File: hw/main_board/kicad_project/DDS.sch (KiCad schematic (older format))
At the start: 0 parts

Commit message: refactored schematic, finalized gain/range
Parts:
- added C? (x5): 0.1uF, symbol C
- added C? (x2): 1uF, symbol C
- added C?: 0.01uF, symbol C
- added C? (x2): 20pF, symbol C
- added DDS?: AD9838, symbol AD9838
- added R?: 20K, symbol R
- added R? (x2): 137R, symbol R
- added RV?: 1K, symbol POT
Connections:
- new net: C?.2, DDS?.3 (DCAP/2.5V)
- new net: C?.1, DDS?.20 (COMP)
- new net: C?.2, DDS?.18 (FSADJUST), R?.1
- new net: C?.1, DDS?.19 (REFOUT)
- new net: R?.2, RV?.1, RV?.2
- new net AGND: C?.1, C?.1, C?.1, C?.1, C?.1, C?.2, C?.2, C?.2, C?.2, DDS?.15 (AGND), DDS?.4 (DGND), R?.1, R?.1, RV?.3
- new net AVDD_3V3: C?.2, C?.2, C?.2, DDS?.1 (AVDD)
- new net CLK_IN: DDS?.5 (MCLK)
- new net DDS_BUS0: DDS?.10 (SDATA)
- new net DDS_BUS1: DDS?.11 (SCLK)
- new net DDS_BUS2: DDS?.12 (FSYNC)
- new net DDS_BUS3: DDS?.6 (FSELECT)
- new net DDS_BUS4: DDS?.7 (PSELECT)
- new net DDS_BUS5: DDS?.8 (RESET)
- new net DDS_BUS6: DDS?.9 (SLEEP)
- new net DVDD_3V3: C?.1, C?.2, DDS?.2 (DVDD)
- new net VOut: C?.1, DDS?.16 (IOUT), R?.2
- new net VOut-: C?.1, DDS?.17 (IOUTB), R?.2

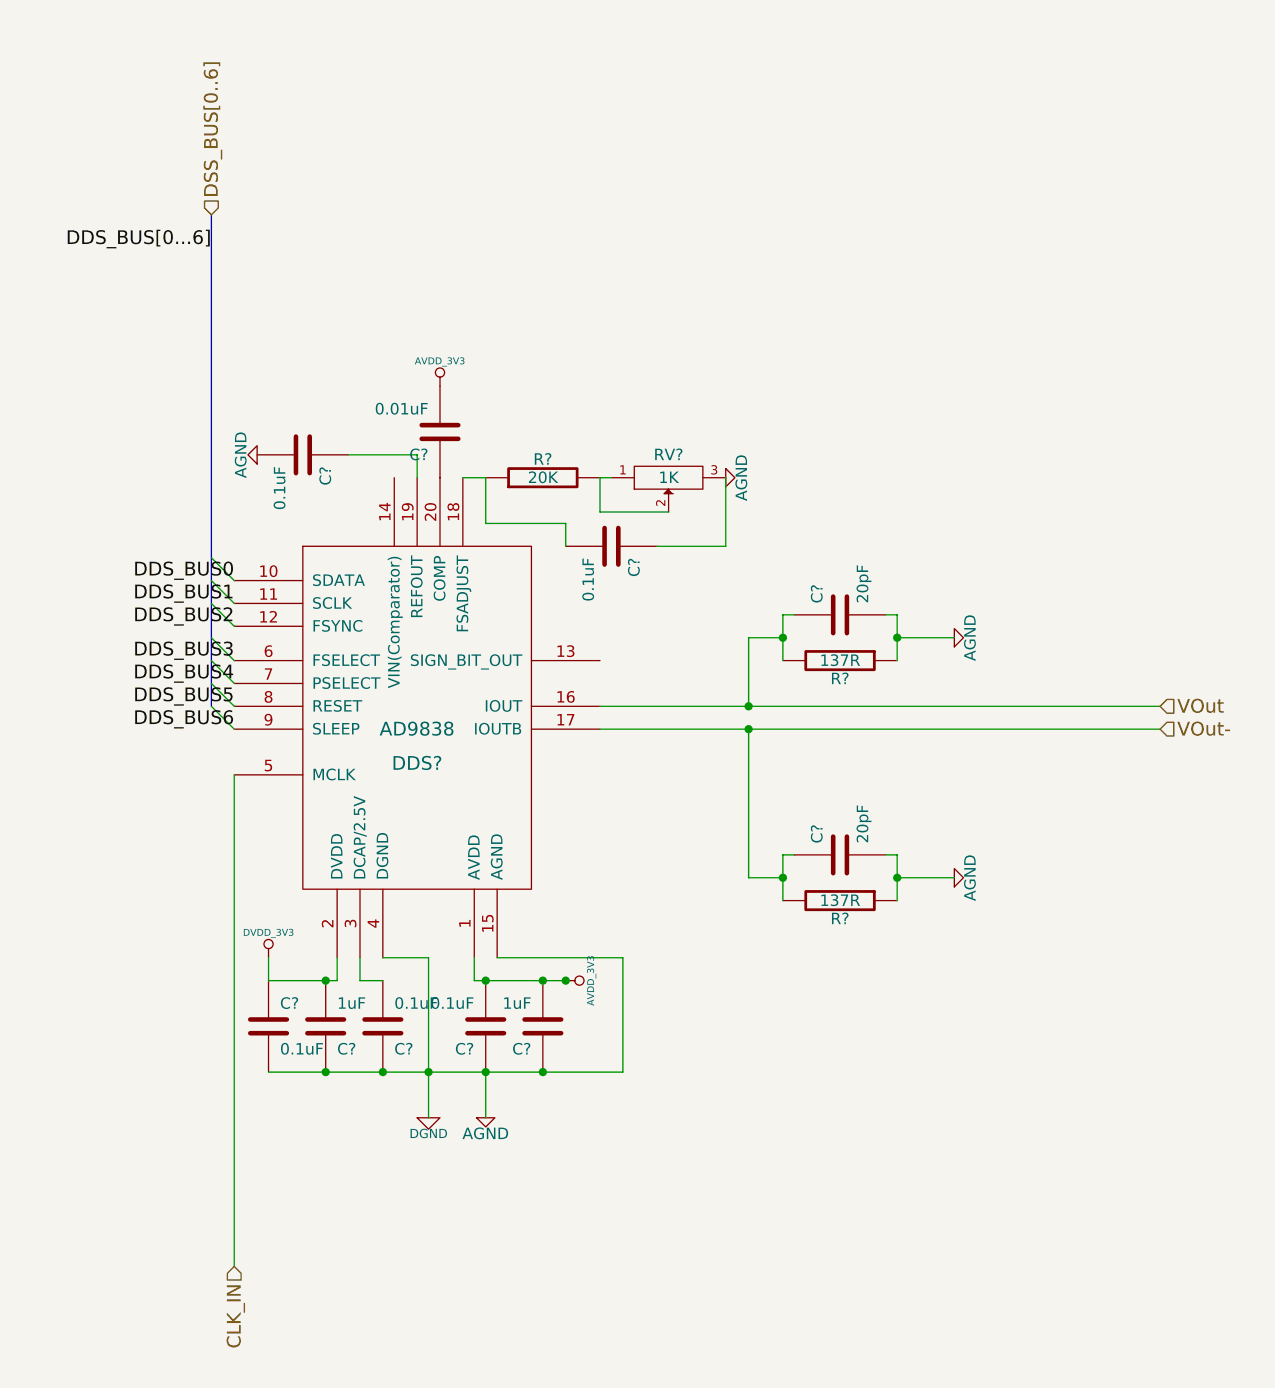
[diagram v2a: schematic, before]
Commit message: started mainboard pcb layout, fixing small things in schematic, TODO: schematic connector symbols and pads
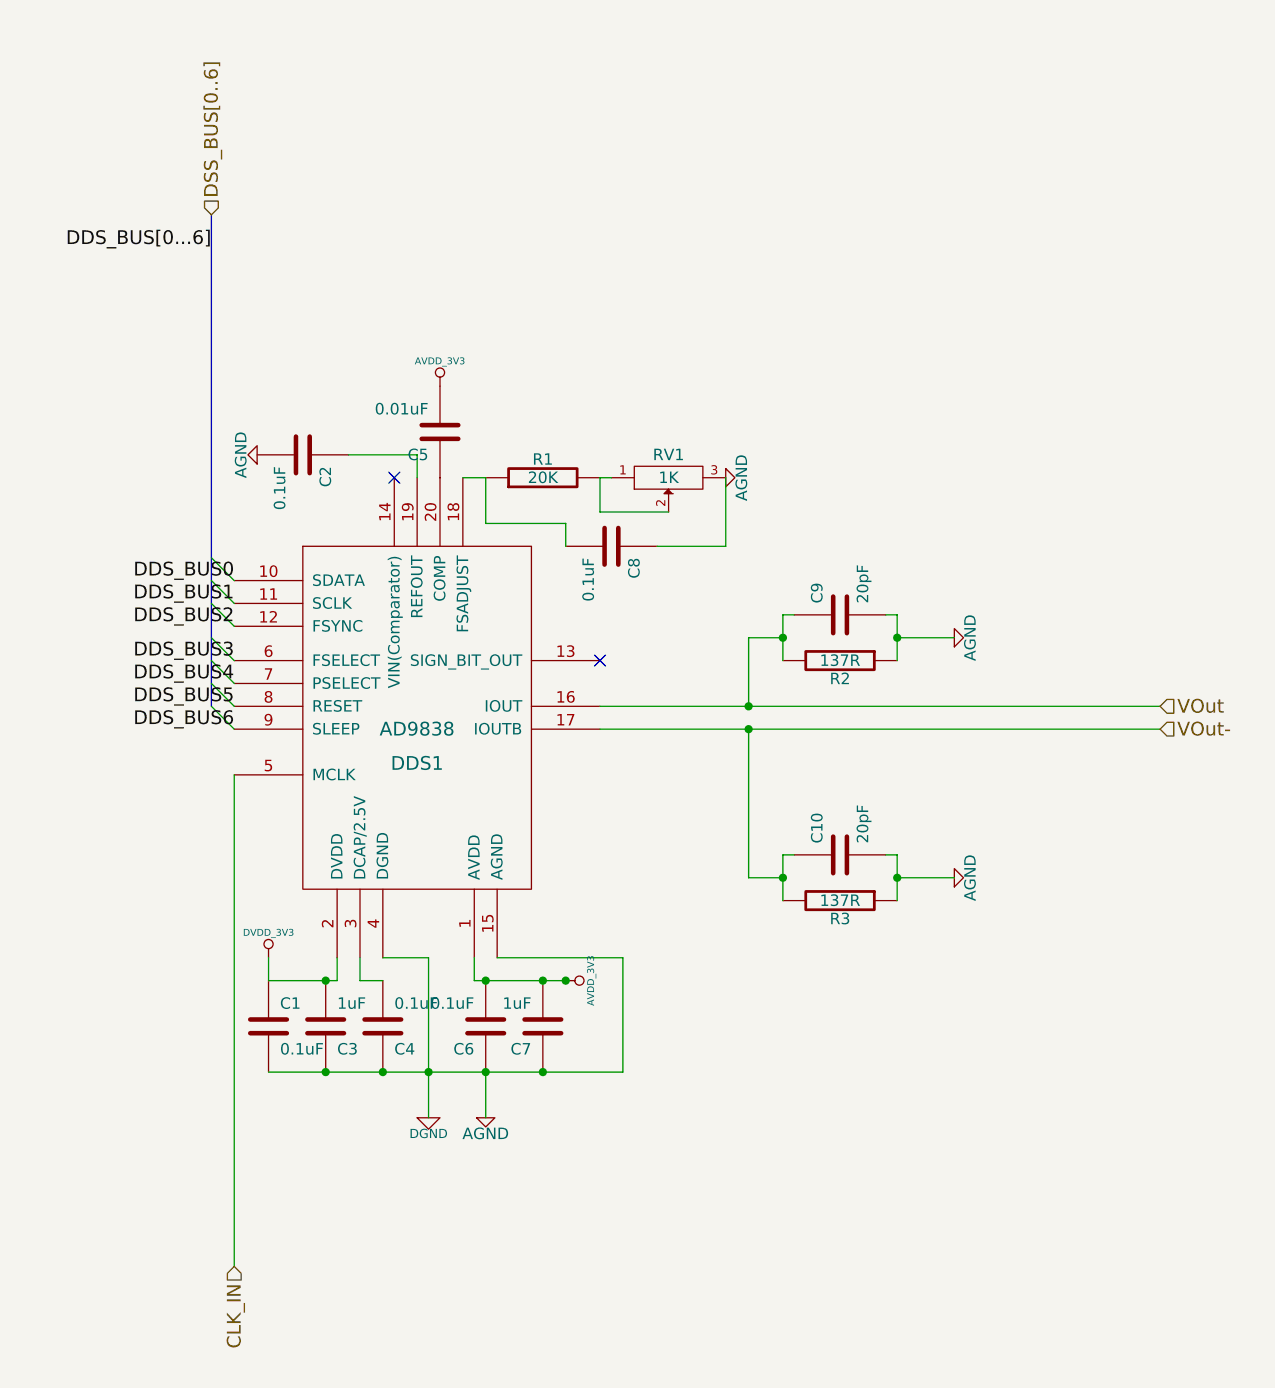
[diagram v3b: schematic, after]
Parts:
- C1, C10, C2, C3, C4, C5, C6, C7, C8, C9: renamed from C?; footprint (none) -> 0603
- DDS1: renamed from DDS?; footprint (none) -> LFCSP20_WQ
- R1, R2, R3: renamed from R?; footprint (none) -> 0603
- RV1: renamed from RV?; footprint (none) -> 3224X
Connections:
- no-connect marks 0 -> 2
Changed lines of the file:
@@
 encoding utf-8
 Sheet 4 7
-Title ""
-Date ""
-Rev ""
+Title "DDS Stage"
+Date "01 Feb 2014"
+Rev "A"
 Comp ""
-Comment1 ""
+Comment1 "Copyright 2014 Andrey Shmakov"
 Comment2 ""
 Comment3 ""
@@
 	5700 4650 5700 5350
 $Comp
-L AGND #PWR?
+L AGND #PWR018
 U 1 1 53166330
 P 5950 5350
-F 0 "#PWR?" H 5950 5350 40  0001 C CNN
+F 0 "#PWR018" H 5950 5350 40  0001 C CNN
 F 1 "AGND" H 5950 5280 50  0000 C CNN
 F 2 "" H 5950 5350 60  0001 C CNN
@@
 $EndComp
 $Comp
-L DGND #PWR?
+L DGND #PWR019
 U 1 1 53166336
 P 5700 5350
-F 0 "#PWR?" H 5700 5350 40  0001 C CNN
+F 0 "#PWR019" H 5700 5350 40  0001 C CNN
 F 1 "DGND" H 5700 5280 40  0000 C CNN
 F 2 "" H 5700 5350 60  0001 C CNN
@@
 $EndComp
 $Comp
-L AVDD_3V3 #PWR?
+L AVDD_3V3 #PWR020
 U 1 1 5316633C
 P 6300 4750
-F 0 "#PWR?" H 6300 4850 30  0001 C CNN
+F 0 "#PWR020" H 6300 4850 30  0001 C CNN
 F 1 "AVDD_3V3" H 6300 4860 30  0000 C CNN
 F 2 "" H 6300 4750 60  0001 C CNN
@@
 $EndComp
 $Comp
-L DVDD_3V3 #PWR?
+L DVDD_3V3 #PWR021
 U 1 1 53166342
 P 5000 4650
-F 0 "#PWR?" H 5000 4750 30  0001 C CNN
+F 0 "#PWR021" H 5000 4750 30  0001 C CNN
 F 1 "DVDD_3V3" H 5000 4760 30  0000 C CNN
 F 2 "" H 5000 4650 60  0001 C CNN
@@
 $EndComp
 $Comp
-L C C?
+L C C4
 U 1 1 53166348
 P 5500 4950
-F 0 "C?" H 5550 5050 50  0000 L CNN
+F 0 "C4" H 5550 5050 50  0000 L CNN
 F 1 "0.1uF" H 5550 4850 50  0000 L CNN
-F 2 "" H 5500 4950 60  0001 C CNN
+F 2 "0603" H 5500 4950 60  0001 C CNN
 F 3 "" H 5500 4950 60  0001 C CNN
 	1    5500 4950
@@
 $EndComp
 $Comp
-L C C?
+L C C3
 U 1 1 5316634E
 P 5250 4950
-F 0 "C?" H 5300 5050 50  0000 L CNN
+F 0 "C3" H 5300 5050 50  0000 L CNN
 F 1 "1uF" H 5300 4850 50  0000 L CNN
-F 2 "" H 5250 4950 60  0001 C CNN
+F 2 "0603" H 5250 4950 60  0001 C CNN
 F 3 "" H 5250 4950 60  0001 C CNN
 	1    5250 4950
@@
 $EndComp
 $Comp
-L C C?
+L C C1
 U 1 1 53166354
 P 5000 4950
-F 0 "C?" H 5050 5050 50  0000 L CNN
+F 0 "C1" H 5050 5050 50  0000 L CNN
 F 1 "0.1uF" H 5050 4850 50  0000 L CNN
-F 2 "" H 5000 4950 60  0001 C CNN
+F 2 "0603" H 5000 4950 60  0001 C CNN
 F 3 "" H 5000 4950 60  0001 C CNN
 	1    5000 4950
@@
 $EndComp
 $Comp
-L AVDD_3V3 #PWR?
+L AVDD_3V3 #PWR022
 U 1 1 5316635A
 P 5750 2150
-F 0 "#PWR?" H 5750 2250 30  0001 C CNN
+F 0 "#PWR022" H 5750 2250 30  0001 C CNN
 F 1 "AVDD_3V3" H 5750 2260 30  0000 C CNN
 F 2 "" H 5750 2150 60  0001 C CNN
@@
 $EndComp
 $Comp
-L C C?
+L C C5
 U 1 1 53166360
 P 5750 2350
-F 0 "C?" H 5800 2450 50  0000 L CNN
+F 0 "C5" H 5800 2450 50  0000 L CNN
 F 1 "0.01uF" H 5800 2250 50  0000 L CNN
-F 2 "" H 5750 2350 60  0001 C CNN
+F 2 "0603" H 5750 2350 60  0001 C CNN
 F 3 "" H 5750 2350 60  0001 C CNN
 	1    5750 2350
@@
 $EndComp
 $Comp
-L C C?
+L C C7
 U 1 1 53166372
 P 6200 4950
-F 0 "C?" H 6250 5050 50  0000 L CNN
+F 0 "C7" H 6250 5050 50  0000 L CNN
 F 1 "1uF" H 6250 4850 50  0000 L CNN
-F 2 "" H 6200 4950 60  0001 C CNN
+F 2 "0603" H 6200 4950 60  0001 C CNN
 F 3 "" H 6200 4950 60  0001 C CNN
 	1    6200 4950
@@
 $EndComp
 $Comp
-L C C?
+L C C6
 U 1 1 53166378
 P 5950 4950
-F 0 "C?" H 6000 5050 50  0000 L CNN
+F 0 "C6" H 6000 5050 50  0000 L CNN
 F 1 "0.1uF" H 6000 4850 50  0000 L CNN
-F 2 "" H 5950 4950 60  0001 C CNN
+F 2 "0603" H 5950 4950 60  0001 C CNN
 F 3 "" H 5950 4950 60  0001 C CNN
 	1    5950 4950
@@
 Connection ~ 6300 4750
 $Comp
-L R R?
+L R R1
 U 1 1 531663A9
 P 6200 2550
-F 0 "R?" V 6280 2550 50  0000 C CNN
+F 0 "R1" V 6280 2550 50  0000 C CNN
 F 1 "20K" V 6200 2550 50  0000 C CNN
-F 2 "" H 6200 2550 60  0001 C CNN
+F 2 "0603" H 6200 2550 60  0001 C CNN
 F 3 "" H 6200 2550 60  0001 C CNN
 	1    6200 2550
@@
 $EndComp
 $Comp
-L POT RV?
+L POT RV1
 U 1 1 531663AF
 P 6750 2550
-F 0 "RV?" H 6750 2450 50  0000 C CNN
+F 0 "RV1" H 6750 2450 50  0000 C CNN
 F 1 "1K" H 6750 2550 50  0000 C CNN
-F 2 "" H 6750 2550 60  0001 C CNN
+F 2 "3224X" H 6750 2550 60  0001 C CNN
 F 3 "" H 6750 2550 60  0001 C CNN
 	1    6750 2550
@@
 	6450 2700 6450 2550
 $Comp
-L AGND #PWR?
+L AGND #PWR023
 U 1 1 531663B9
 P 7000 2550
-F 0 "#PWR?" H 7000 2550 40  0001 C CNN
+F 0 "#PWR023" H 7000 2550 40  0001 C CNN
 F 1 "AGND" H 7000 2480 50  0000 C CNN
 F 2 "" H 7000 2550 60  0001 C CNN
@@
 $EndComp
 $Comp
-L C C?
+L C C8
 U 1 1 531663BF
 P 6500 2850
-F 0 "C?" H 6550 2950 50  0000 L CNN
+F 0 "C8" H 6550 2950 50  0000 L CNN
 F 1 "0.1uF" H 6550 2750 50  0000 L CNN
-F 2 "" H 6500 2850 60  0001 C CNN
+F 2 "0603" H 6500 2850 60  0001 C CNN
 F 3 "" H 6500 2850 60  0001 C CNN
 	1    6500 2850
@@
 	7000 2850 7000 2550
 $Comp
-L C C?
+L C C2
 U 1 1 531663CA
 P 5150 2450
-F 0 "C?" H 5200 2550 50  0000 L CNN
+F 0 "C2" H 5200 2550 50  0000 L CNN
 F 1 "0.1uF" H 5200 2350 50  0000 L CNN
-F 2 "" H 5150 2450 60  0001 C CNN
+F 2 "0603" H 5150 2450 60  0001 C CNN
 F 3 "" H 5150 2450 60  0001 C CNN
 	1    5150 2450
@@
 	5650 2450 5350 2450
 $Comp
-L AGND #PWR?
+L AGND #PWR024
 U 1 1 531663D2
 P 4950 2450
-F 0 "#PWR?" H 4950 2450 40  0001 C CNN
+F 0 "#PWR024" H 4950 2450 40  0001 C CNN
 F 1 "AGND" H 4950 2380 50  0000 C CNN
 F 2 "" H 4950 2450 60  0001 C CNN
@@
 DSS_BUS[0..6]
 $Comp
-L C C?
+L C C9
 U 1 1 53166A22
 P 7500 3150
-F 0 "C?" H 7550 3250 50  0000 L CNN
+F 0 "C9" H 7550 3250 50  0000 L CNN
 F 1 "20pF" H 7550 3050 50  0000 L CNN
-F 2 "" H 7500 3150 60  0001 C CNN
+F 2 "0603" H 7500 3150 60  0001 C CNN
 F 3 "" H 7500 3150 60  0001 C CNN
 	1    7500 3150
@@
 $EndComp
 $Comp
-L AGND #PWR?
+L AGND #PWR025
 U 1 1 53166A28
 P 8000 3250
-F 0 "#PWR?" H 8000 3250 40  0001 C CNN
+F 0 "#PWR025" H 8000 3250 40  0001 C CNN
 F 1 "AGND" H 8000 3180 50  0000 C CNN
 F 2 "" H 8000 3250 60  0001 C CNN
@@
 $EndComp
 $Comp
-L R R?
+L R R2
 U 1 1 53166A2E
 P 7500 3350
-F 0 "R?" V 7580 3350 50  0000 C CNN
+F 0 "R2" V 7580 3350 50  0000 C CNN
 F 1 "137R" V 7500 3350 50  0000 C CNN
-F 2 "" H 7500 3350 60  0001 C CNN
+F 2 "0603" H 7500 3350 60  0001 C CNN
 F 3 "" H 7500 3350 60  0001 C CNN
 	1    7500 3350
@@
 Connection ~ 7750 3250
 $Comp
-L C C?
+L C C10
 U 1 1 53166A3C
 P 7500 4200
-F 0 "C?" H 7550 4300 50  0000 L CNN
+F 0 "C10" H 7550 4300 50  0000 L CNN
 F 1 "20pF" H 7550 4100 50  0000 L CNN
-F 2 "" H 7500 4200 60  0001 C CNN
+F 2 "0603" H 7500 4200 60  0001 C CNN
 F 3 "" H 7500 4200 60  0001 C CNN
 	1    7500 4200
@@
 $EndComp
 $Comp
-L AGND #PWR?
+L AGND #PWR026
 U 1 1 53166A42
 P 8000 4300
-F 0 "#PWR?" H 8000 4300 40  0001 C CNN
+F 0 "#PWR026" H 8000 4300 40  0001 C CNN
 F 1 "AGND" H 8000 4230 50  0000 C CNN
 F 2 "" H 8000 4300 60  0001 C CNN
@@
 $EndComp
 $Comp
-L R R?
+L R R3
 U 1 1 53166A48
 P 7500 4400
-F 0 "R?" V 7580 4400 50  0000 C CNN
+F 0 "R3" V 7580 4400 50  0000 C CNN
 F 1 "137R" V 7500 4400 50  0000 C CNN
-F 2 "" H 7500 4400 60  0001 C CNN
+F 2 "0603" H 7500 4400 60  0001 C CNN
 F 3 "" H 7500 4400 60  0001 C CNN
 	1    7500 4400
@@
 Connection ~ 7750 4300
 $Comp
-L AD9838 DDS?
+L AD9838 DDS1
 U 1 1 53166398
 P 5650 3600
-F 0 "DDS?" H 5650 3400 60  0000 C CNN
+F 0 "DDS1" H 5650 3400 60  0000 C CNN
 F 1 "AD9838" H 5650 3550 60  0000 C CNN
-F 2 "" H 5650 3600 60  0001 C CNN
+F 2 "LFCSP20_WQ" H 5650 3600 60  0001 C CNN
 F 3 "" H 5650 3600 60  0001 C CNN
 	1    5650 3600
@@
 Text HLabel 8900 3650 2    60   Input ~ 0
 VOut-
+NoConn ~ 6450 3350
+NoConn ~ 5550 2550
 $EndSCHEMATC

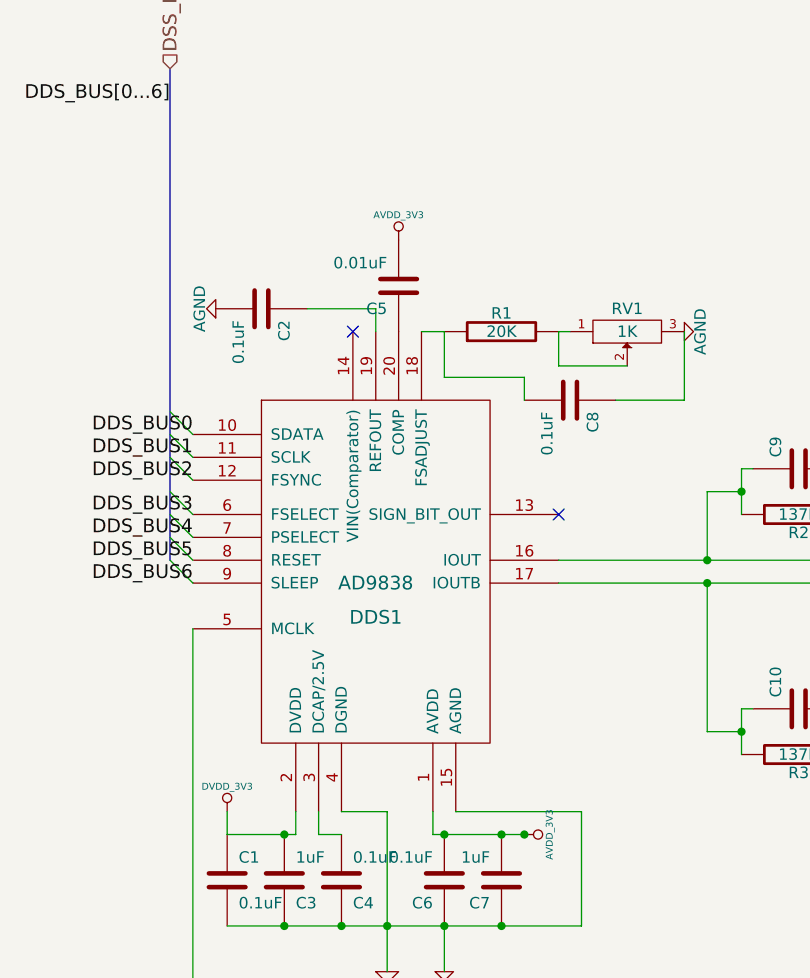
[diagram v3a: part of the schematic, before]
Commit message: final rework of mux board, finalizing stacking connectors, almost there
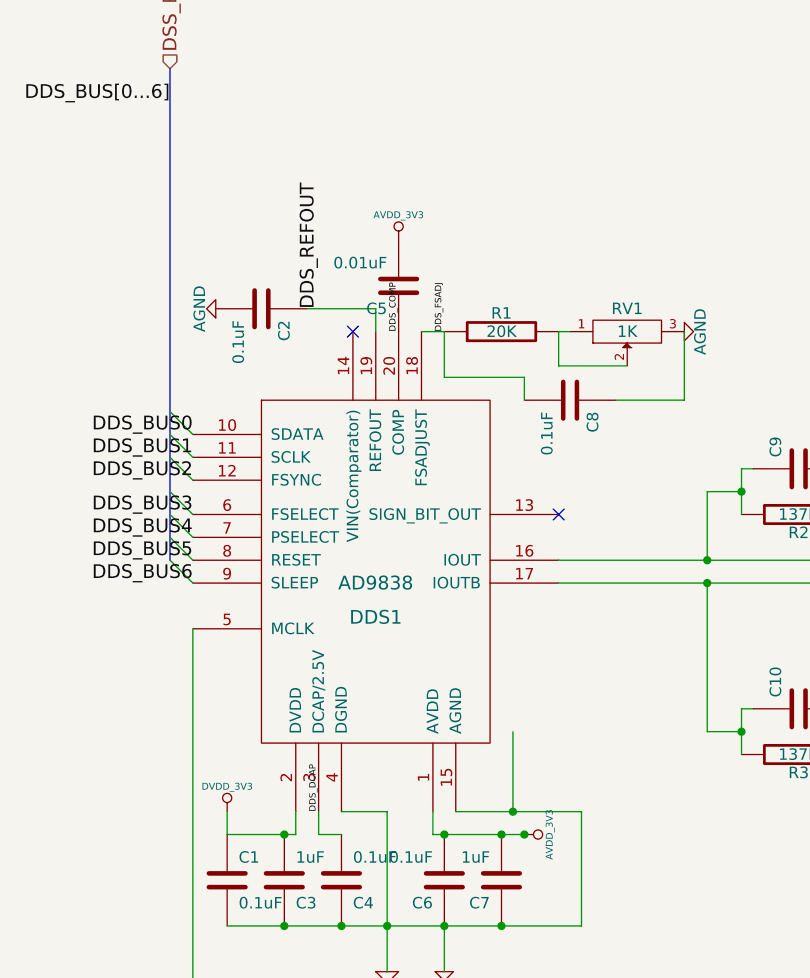
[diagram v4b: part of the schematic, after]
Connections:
- net DDS_DCAP: now reaches C4.2, DDS1.3 (DCAP/2.5V)
- net DDS_COMP: now reaches C5.1, DDS1.20 (COMP)
- net DDS_FSADJ: now reaches C8.2, DDS1.18 (FSADJUST), R1.1
- net DDS_REFOUT: now reaches C2.1, DDS1.19 (REFOUT)
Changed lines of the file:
@@
 EESchema Schematic File Version 2
-LIBS:power
-LIBS:device
-LIBS:transistors
-LIBS:conn
-LIBS:linear
-LIBS:regul
-LIBS:74xx
-LIBS:cmos4000
-LIBS:adc-dac
-LIBS:memory
-LIBS:xilinx
-LIBS:special
-LIBS:microcontrollers
-LIBS:dsp
-LIBS:microchip
-LIBS:analog_switches
-LIBS:motorola
-LIBS:texas
-LIBS:intel
-LIBS:audio
-LIBS:interface
-LIBS:digital-audio
-LIBS:philips
-LIBS:display
-LIBS:cypress
-LIBS:siliconi
-LIBS:opto
-LIBS:atmel
-LIBS:contrib
-LIBS:valves
 LIBS:ddslib
-LIBS:demuxcomplib
-LIBS:tdsc-kicad-convert
 LIBS:tDCS_driver-cache
 EELAYER 24 0
@@
 	5700 4650 5700 5350
 $Comp
-L AGND #PWR018
+L AGND #PWR024
 U 1 1 53166330
 P 5950 5350
-F 0 "#PWR018" H 5950 5350 40  0001 C CNN
+F 0 "#PWR024" H 5950 5350 40  0001 C CNN
 F 1 "AGND" H 5950 5280 50  0000 C CNN
 F 2 "" H 5950 5350 60  0001 C CNN
@@
 $EndComp
 $Comp
-L DGND #PWR019
+L DGND #PWR025
 U 1 1 53166336
 P 5700 5350
-F 0 "#PWR019" H 5700 5350 40  0001 C CNN
+F 0 "#PWR025" H 5700 5350 40  0001 C CNN
 F 1 "DGND" H 5700 5280 40  0000 C CNN
 F 2 "" H 5700 5350 60  0001 C CNN
@@
 $EndComp
 $Comp
-L AVDD_3V3 #PWR020
+L AVDD_3V3 #PWR026
 U 1 1 5316633C
 P 6300 4750
-F 0 "#PWR020" H 6300 4850 30  0001 C CNN
+F 0 "#PWR026" H 6300 4850 30  0001 C CNN
 F 1 "AVDD_3V3" H 6300 4860 30  0000 C CNN
 F 2 "" H 6300 4750 60  0001 C CNN
@@
 $EndComp
 $Comp
-L DVDD_3V3 #PWR021
+L DVDD_3V3 #PWR027
 U 1 1 53166342
 P 5000 4650
-F 0 "#PWR021" H 5000 4750 30  0001 C CNN
+F 0 "#PWR027" H 5000 4750 30  0001 C CNN
 F 1 "DVDD_3V3" H 5000 4760 30  0000 C CNN
 F 2 "" H 5000 4650 60  0001 C CNN
@@
 $EndComp
 $Comp
-L AVDD_3V3 #PWR022
+L AVDD_3V3 #PWR028
 U 1 1 5316635A
 P 5750 2150
-F 0 "#PWR022" H 5750 2250 30  0001 C CNN
+F 0 "#PWR028" H 5750 2250 30  0001 C CNN
 F 1 "AVDD_3V3" H 5750 2260 30  0000 C CNN
 F 2 "" H 5750 2150 60  0001 C CNN
@@
 	6450 2700 6450 2550
 $Comp
-L AGND #PWR023
+L AGND #PWR029
 U 1 1 531663B9
 P 7000 2550
-F 0 "#PWR023" H 7000 2550 40  0001 C CNN
+F 0 "#PWR029" H 7000 2550 40  0001 C CNN
 F 1 "AGND" H 7000 2480 50  0000 C CNN
 F 2 "" H 7000 2550 60  0001 C CNN
@@
 	5650 2450 5350 2450
 $Comp
-L AGND #PWR024
+L AGND #PWR030
 U 1 1 531663D2
 P 4950 2450
-F 0 "#PWR024" H 4950 2450 40  0001 C CNN
+F 0 "#PWR030" H 4950 2450 40  0001 C CNN
 F 1 "AGND" H 4950 2380 50  0000 C CNN
 F 2 "" H 4950 2450 60  0001 C CNN
@@
 $EndComp
 $Comp
-L AGND #PWR025
+L AGND #PWR031
 U 1 1 53166A28
 P 8000 3250
-F 0 "#PWR025" H 8000 3250 40  0001 C CNN
+F 0 "#PWR031" H 8000 3250 40  0001 C CNN
 F 1 "AGND" H 8000 3180 50  0000 C CNN
 F 2 "" H 8000 3250 60  0001 C CNN
@@
 $EndComp
 $Comp
-L AGND #PWR026
+L AGND #PWR032
 U 1 1 53166A42
 P 8000 4300
-F 0 "#PWR026" H 8000 4300 40  0001 C CNN
+F 0 "#PWR032" H 8000 4300 40  0001 C CNN
 F 1 "AGND" H 8000 4230 50  0000 C CNN
 F 2 "" H 8000 4300 60  0001 C CNN
@@
 NoConn ~ 6450 3350
 NoConn ~ 5550 2550
+Text Label 5400 2450 1    60   ~ 0
+DDS_REFOUT
+Text Label 5750 2550 1    28   ~ 0
+DDS_COMP
+Text Label 5950 2550 1    28   ~ 0
+DDS_FSADJ
+Text Label 5400 4650 1    28   ~ 0
+DDS_DCAP
+Wire Wire Line
+	6250 4300 6250 4650
+Connection ~ 6250 4650
 $EndSCHEMATC
